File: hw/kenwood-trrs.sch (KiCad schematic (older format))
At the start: 12 parts, among them J1 TRRS Jack, J2 BAOFENG2.5SPK, J3 BAOFENG3.5MIC, Q1 BSS138, Q2 BSS83P

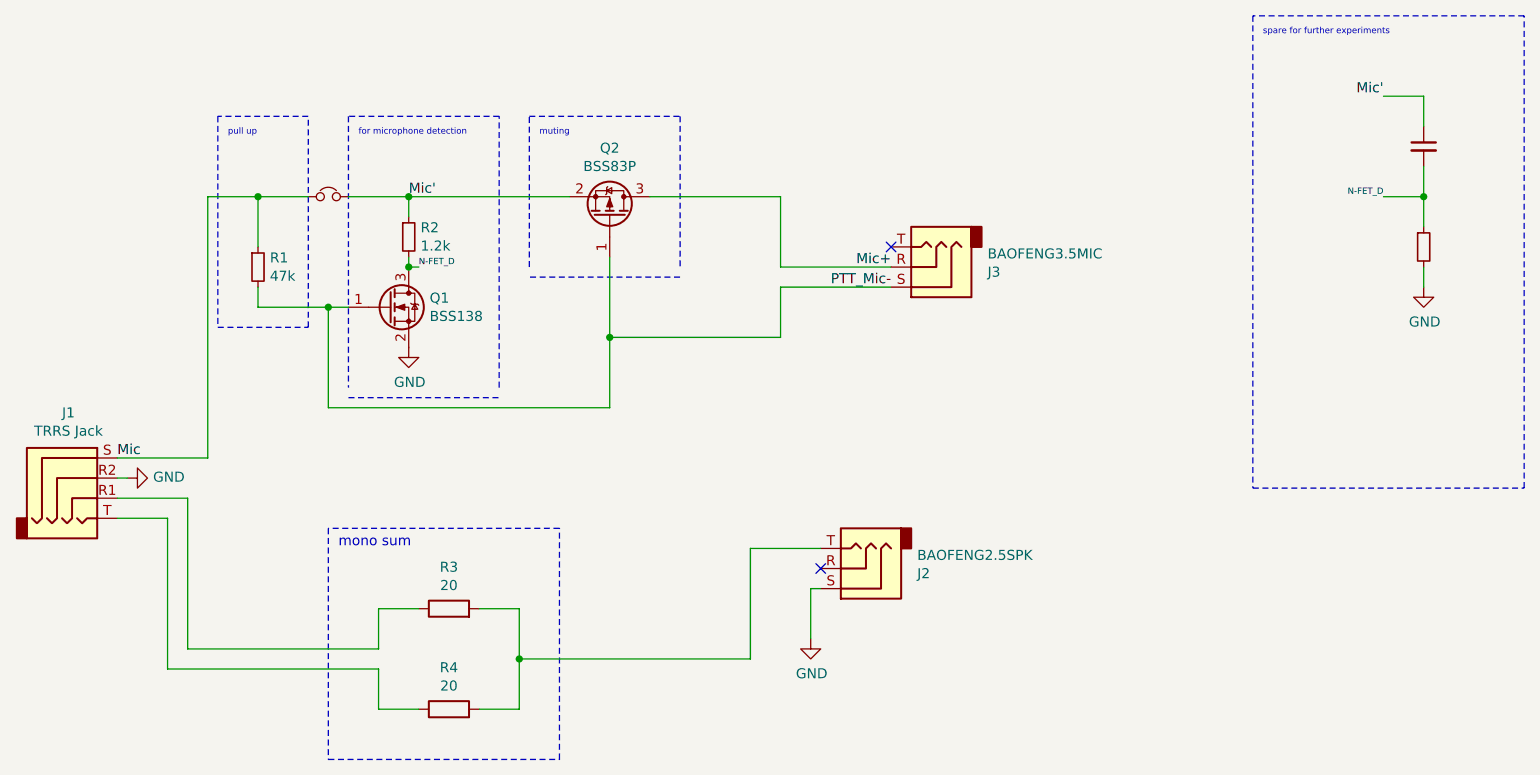
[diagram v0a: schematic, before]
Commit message: new version with different muting mechanism
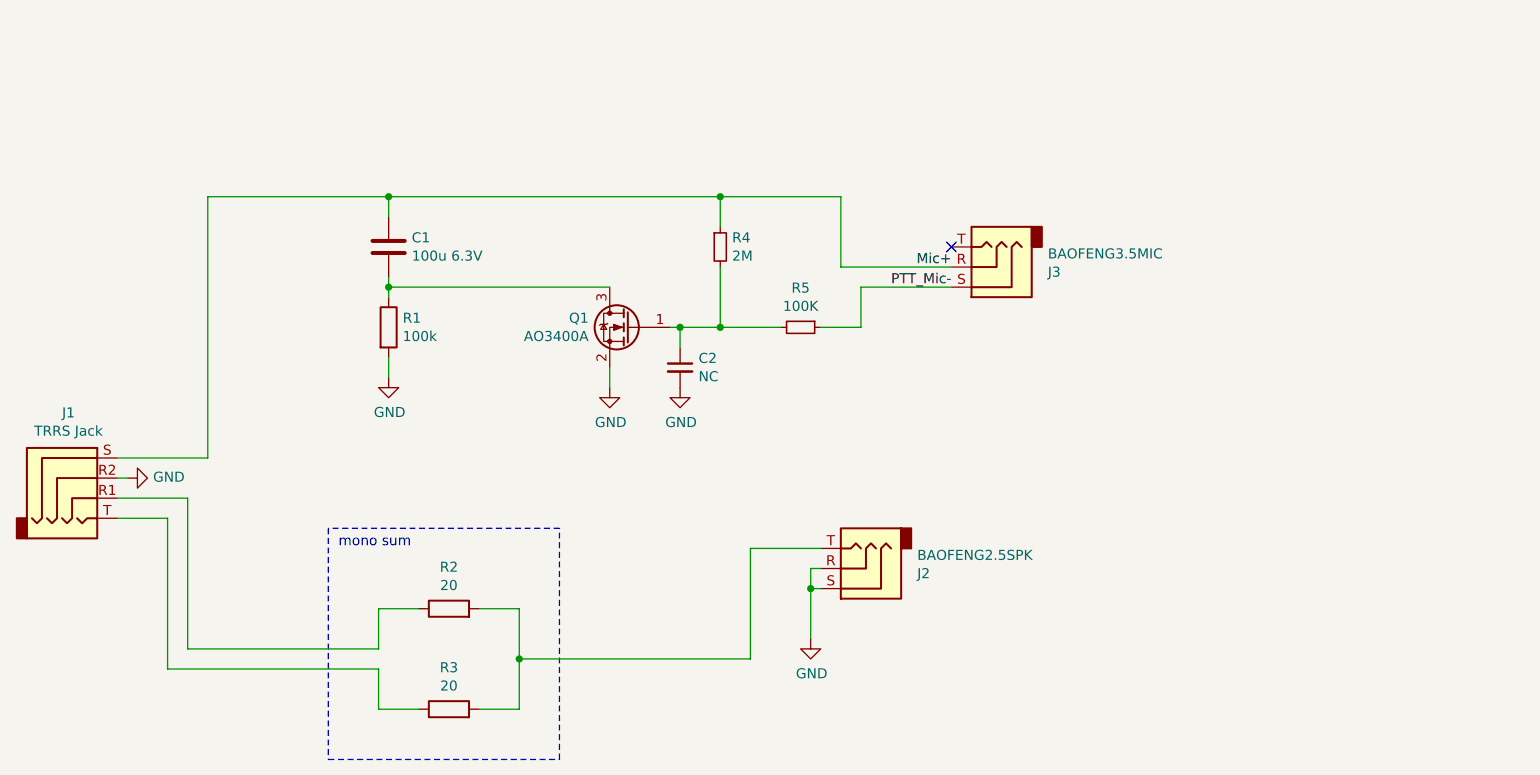
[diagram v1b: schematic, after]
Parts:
- removed C1: C_Small, Capacitor_SMD:C_0805_2012Metric_Pad1.15x1.40mm_HandSolder, symbol Device:C_Small
- removed JP1: Jumper_NC_Small, Jumper:SolderJumper-2_P1.3mm_Bridged_RoundedPad1.0x1.5mm, symbol Device:Jumper_NC_Small
- removed Q1: BSS138, Package_TO_SOT_SMD:SOT-23, symbol Transistor_FET:BSS138
- removed Q2: BSS83P, Package_TO_SOT_SMD:SOT-23, symbol Transistor_FET:BSS83P
- removed R1: 47k, Resistor_SMD:R_0805_2012Metric_Pad1.15x1.40mm_HandSolder, symbol Device:R_Small
- removed R2: 1.2k, Resistor_SMD:R_0805_2012Metric_Pad1.15x1.40mm_HandSolder, symbol Device:R_Small
- added C1: 100u 6.3V, Capacitor_THT:CP_Radial_D5.0mm_P2.00mm, symbol Device:C
- added C2: NC, Capacitor_SMD:C_0805_2012Metric, symbol Device:C_Small
- added Q1: AO3400A, Package_TO_SOT_SMD:SOT-23_Handsoldering, symbol Transistor_FET:AO3400A
- added R1: 100k, Resistor_SMD:R_0805_2012Metric_Pad1.20x1.40mm_HandSolder, symbol Device:R
- added R4: 2M, Resistor_SMD:R_0805_2012Metric_Pad1.20x1.40mm_HandSolder, symbol Device:R_Small
- R5: value R_Small -> 100K; footprint Resistor_SMD:R_0805_2012Metric_Pad1.15x1.40mm_HandSolder -> Resistor_SMD:R_0805_2012Metric_Pad1.20x1.40mm_HandSolder
- renumbered R3 to R2, R4 to R3
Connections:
- net Mic is gone; now on net Mic+: J1.S
- net N-FET_D is gone; now on net PTT_Mic-: R5.1
- net GND: now also J2.R, C2.2, Q1.2 (S), R1.2; no longer R5.2
- net Mic+: now also C1.1, R4.1
- new net: C1.2, Q1.3 (D), R1.1
- new net: C2.1, Q1.1 (G), R4.2, R5.2
- no-connect marks 2 -> 1
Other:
- note removed: "for microphone detection"
- note removed: "muting"
- note removed: "pull up"
- note removed: "spare for further experiments\n"
- moved on the sheet: J3
